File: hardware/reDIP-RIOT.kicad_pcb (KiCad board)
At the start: 4 copper layers, 17.8 x 50.8 mm, 45 parts, among them J1 Conn_01x20, J2 Conn_01x20, J3 Conn_02x05_Odd_Even, U1 NCP115AMX120TCG, U2 NCP115AMX330TCG, U3 SN74CBT16210CDGGR, U4 SN74CBT16210CDGGR, U5 74AHC1G14SE-7, U6 ICE5LP1K-SG48, U7 AT25EU0011A-SSHN-T

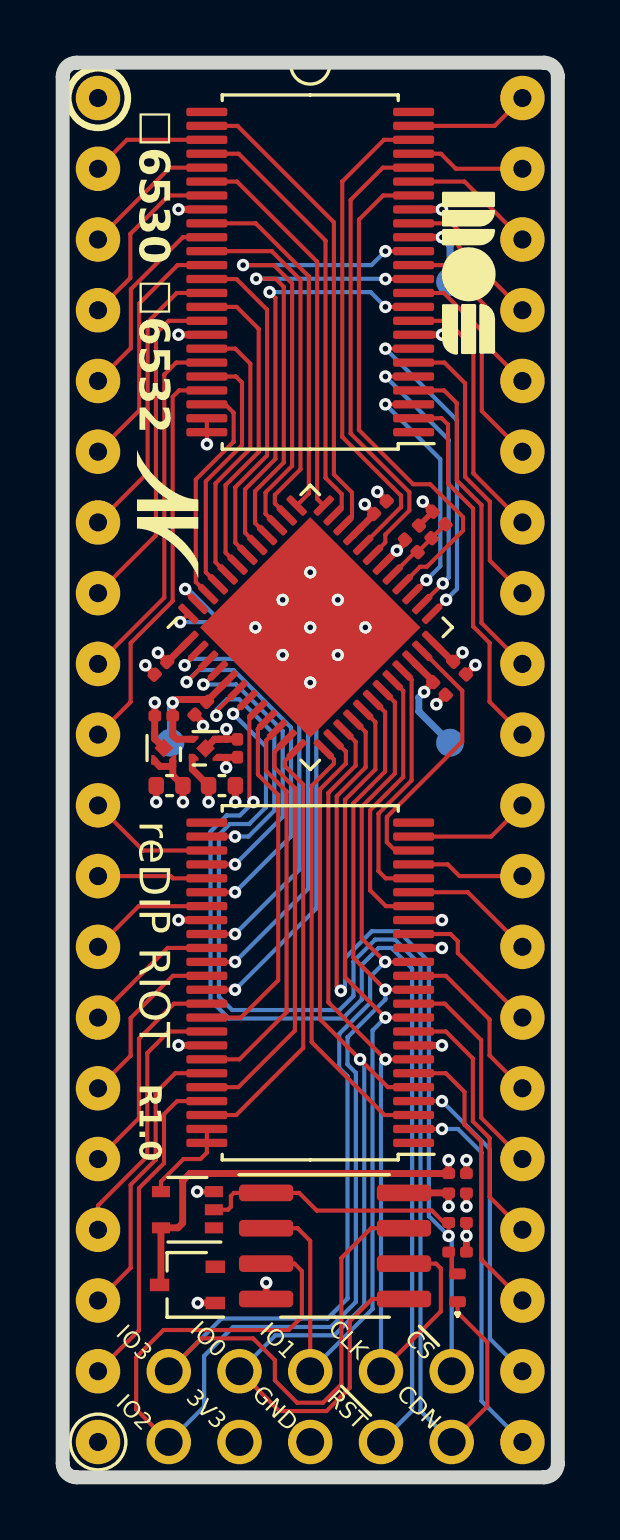
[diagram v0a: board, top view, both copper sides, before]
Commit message: Added CRESET pull-up, removed CDONE LED
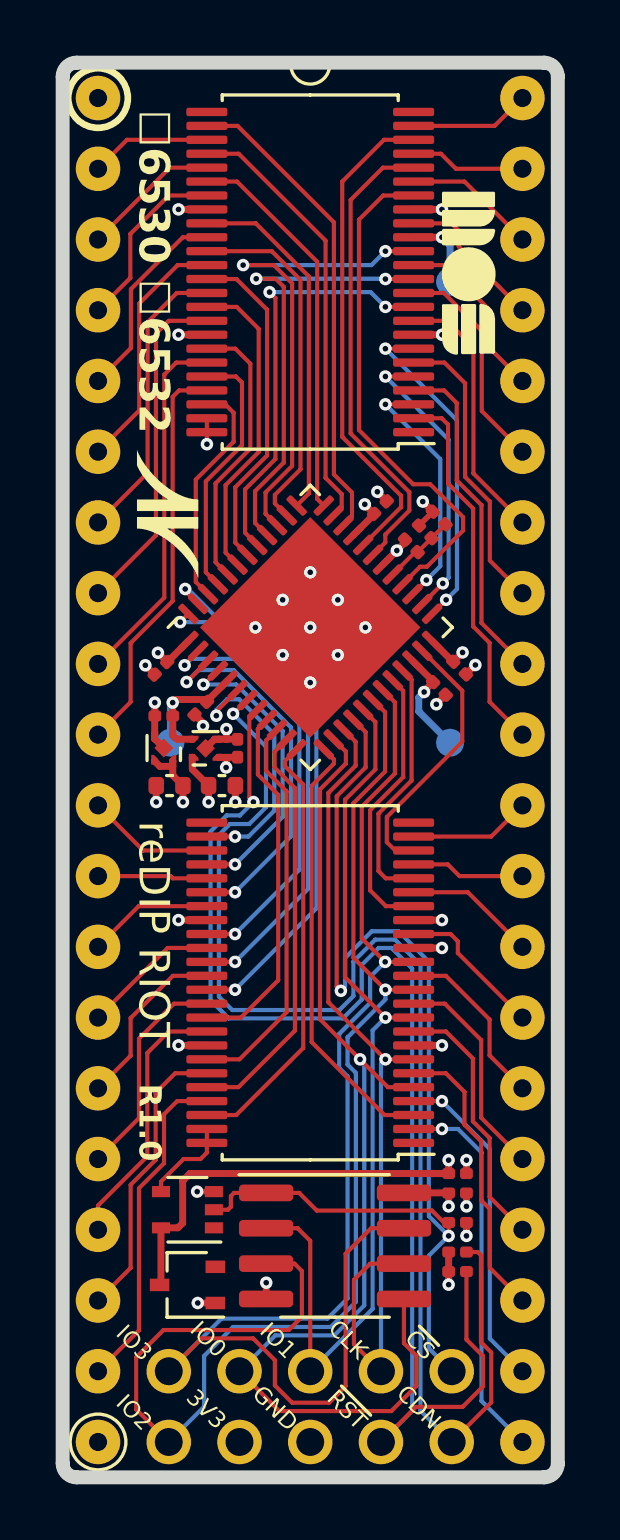
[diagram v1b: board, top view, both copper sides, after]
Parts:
- removed D2: IN-S42BT5B, Inolux:LED_0402_1005Metric
- removed the R3 at (112.9, 141.4)
- added R4: 10k, Resistor_SMD:R_0201_0603Metric, F.Cu at (112.9, 142.1)
- added R5: 2.87k, Resistor_SMD:R_0201_0603Metric, F.Cu at (112.9, 141.4)
- U5: value 74AHC1G14SE-7 -> 74AHC1G14
- renumbered R4 to R3
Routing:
- net /~{CRESET}: track 38.6 -> 47.4 mm
- net /CDONE: track 45.7 -> 47.7 mm
- net /SPI_SIO0: track 38.9 -> 40.0 mm
- net Net-(D2-A): track 0.96 -> 0.00 mm
- net /SPI_~{CS}: track 40.4 -> 41.0 mm
- net +3V3: track 12.8 -> 13.4 mm, vias 7 -> 8

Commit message: Cleanup
* Removed unused footprints
* Rounded rectangle pads for SOT footprints
* Increased drill to 0.8mm for header pins
* Corrected BOM text
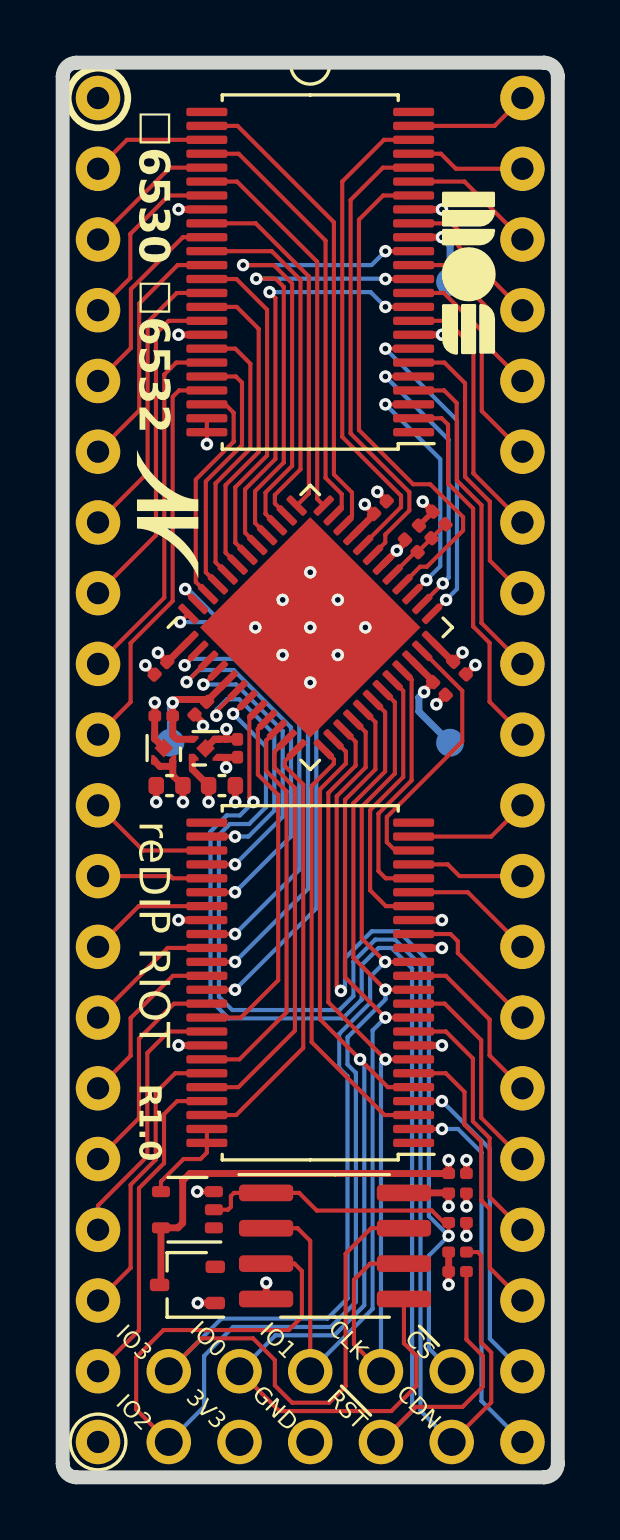
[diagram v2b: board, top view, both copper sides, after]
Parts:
- D1: footprint Package_TO_SOT_SMD:SOT-323_SC-70 -> reDIP:SOT-323_SC-70
- REF**: renamed from svg2mod; value G*** -> Nimrod N
- REF** (x2): renamed from MOS logo; value G*** -> MOS logo
- REF**: renamed from OSHW logo; value G*** -> OSHW logo
- REF**: renamed from svg2mod; value G*** -> Nimrod logo
- U5: footprint Package_TO_SOT_SMD:SOT-353_SC-70-5 -> reDIP:SOT-353_SC-70-5
- U7: value AT25EU0011A-SSHN-T -> AT25EU0011A-SSHN

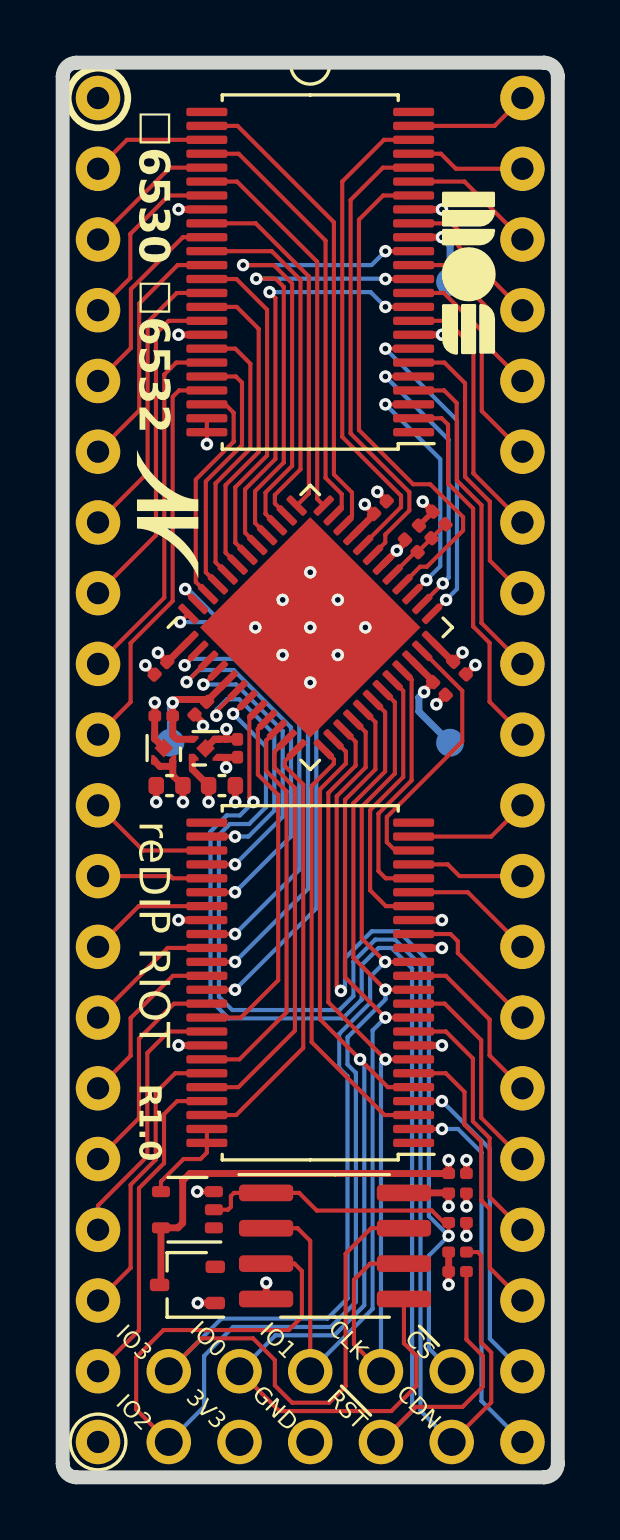
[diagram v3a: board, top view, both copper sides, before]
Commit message: LDO ground planes, via teardrops
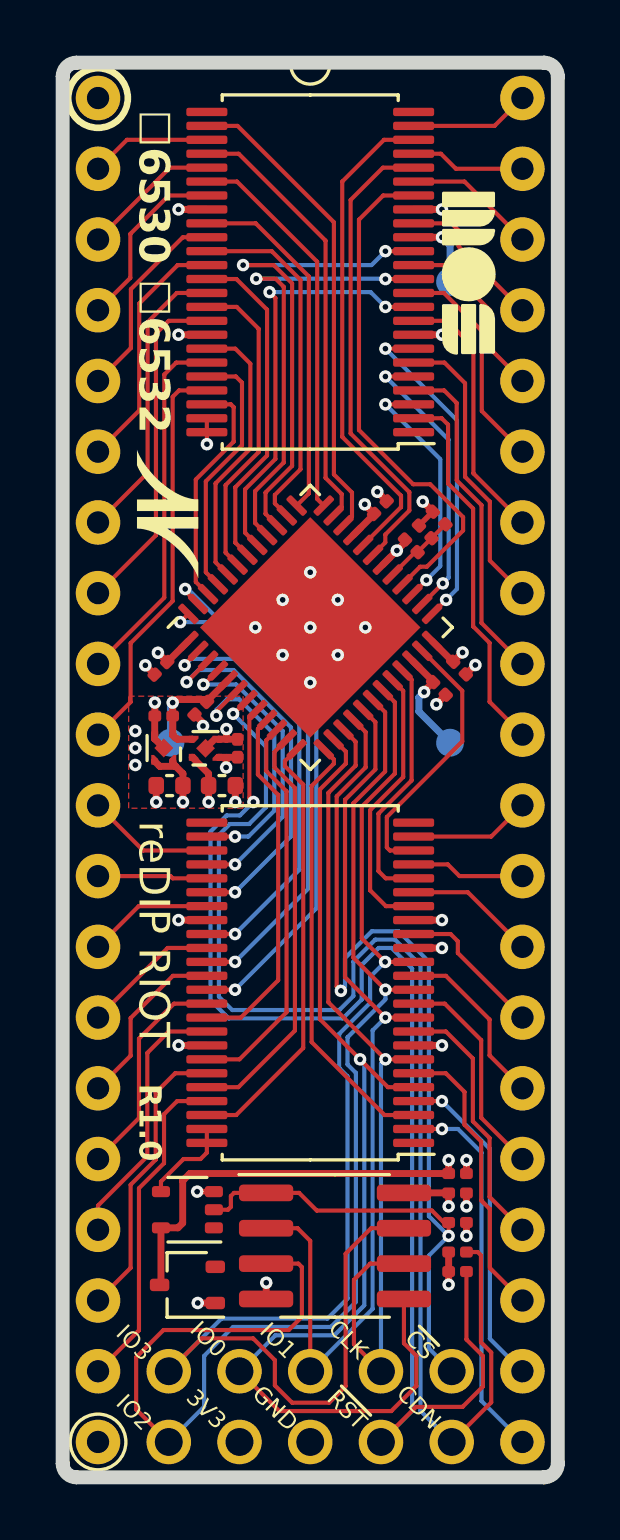
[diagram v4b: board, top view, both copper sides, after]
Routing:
- net GND: track 19.5 -> 19.4 mm, vias 32 -> 35
- added copper zone on F.Cu, net GND

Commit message: Use 74AHCT1G14 for better signal level margins
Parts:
- U5: value 74AHC1G14 -> 74AHCT1G14
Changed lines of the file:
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@@
     (property "Description" "IC SCHMITT-TRIGGER INVERTER")
     (property "Mfg" "Diodes")
-    (property "Notes" "Replacement parts: 74AHC1G14 SOT-353/SC-70-5")
-    (property "PN" "74AHC1G14SE-7")
+    (property "Notes" "Replacement parts: 74AHCT1G14 SOT-353/SC-70-5")
+    (property "PN" "74AHCT1G14SE-7")
     (property "Sheetfile" "reDIP-RIOT.kicad_sch")
     (property "Sheetname" "")
@@
         (effects (font (size 1 1) (thickness 0.15)))
     )
-    (fp_text value "74AHC1G14" (at 0 2) (layer "F.Fab") hide
+    (fp_text value "74AHCT1G14" (at 0 2) (layer "F.Fab") hide
         (effects (font (size 1 1) (thickness 0.15)))
     )

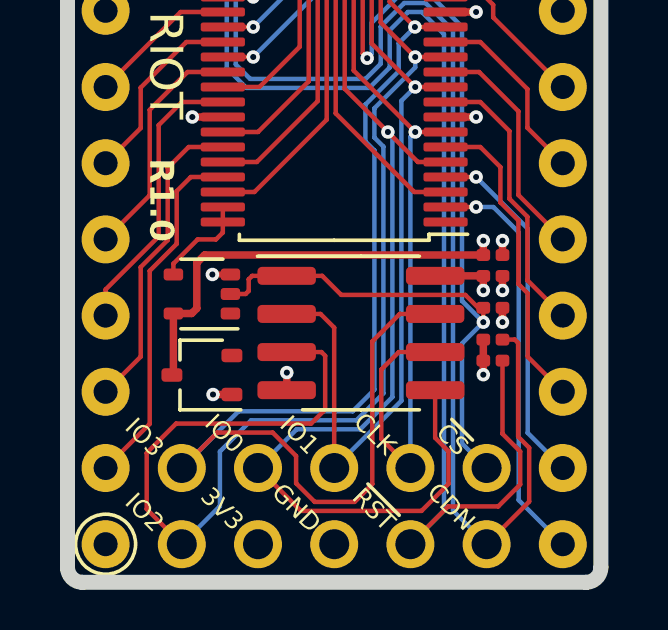
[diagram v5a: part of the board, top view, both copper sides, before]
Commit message: Power supply for 74AHCT1G14 within range
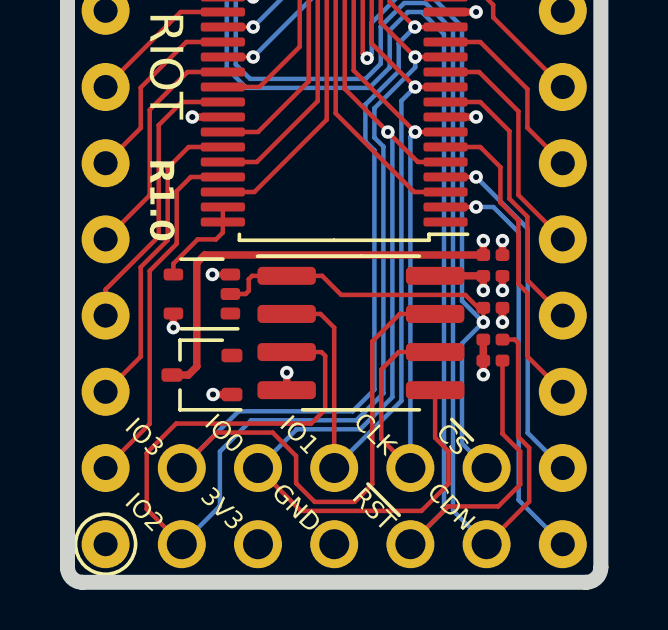
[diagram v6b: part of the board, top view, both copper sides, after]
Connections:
- U5 pad 5: VCBT -> VCC
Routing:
- net VCC: track 32.0 -> 32.3 mm, vias 3 -> 4

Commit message: Replaced iCE5LP1K with iCE40UP5K
The MOS 6530 and MOS 6532 have on-chip data port pull-up resistors
in the range of 5k.

While the iCE40UP5K features configurable 3.3k/6.8k/10k/100k pull-up
resistors, the iCE5LP1K only features 100k pull-up resistors.

We make the simple fix of using the more capable (and somewhat more
expensive) pin compatible iCE40UP5K, instead of adding physical
pull-up resistors to separate boards for the MOS 6530 and MOS 6532.
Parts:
- U6: value ICE5LP1K-SG48 -> ICE40UP5K-SG48
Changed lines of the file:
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@@
     (property "Description" "IC FPGA QFN-48")
     (property "Mfg" "Lattice")
-    (property "PN" "ICE5LP1K-SG48ITR")
+    (property "PN" "ICE40UP5K-SG48I")
     (property "Sheetfile" "reDIP-RIOT.kicad_sch")
     (property "Sheetname" "")
-    (property "ki_description" "iCE40 Ultra FPGA, 1100 LUTs, 1.2V, 48-pin QFN")
+    (property "ki_description" "iCE40 UltraPlus FPGA, 5280 LUTs, 1.2V, 48-pin QFN")
     (property "ki_keywords" "FPGA programmable logic")
     (attr smd)
@@
         (effects (font (size 1 1) (thickness 0.15)))
     )
-    (fp_text value "ICE5LP1K-SG48" (at 0 4.82 45) (layer "F.Fab") hide
+    (fp_text value "ICE40UP5K-SG48" (at 0 4.82 45) (layer "F.Fab") hide
         (effects (font (size 1 1) (thickness 0.15)))
     )
@@
     (pad "" smd roundrect (at 0 0 225) (size 0.38 0.38) (layers "F.Paste") (roundrect_rratio 0.2))
     (pad "1" smd custom (at -0.475 -0.325 90) (size 0.25 0.25) (layers "F.Cu" "F.Paste" "F.Mask")
-      (net 2 "+3V3") (pinfunction "OUT") (pintype "power_out") (zone_connect 2) (thermal_bridge_angle 45)
+      (net 2 "+3V3") (pinfunction "OUT") (pintype "power_out") (zone_connect 2)
       (options (clearance outline) (anchor circle))
       (primitives
@@
       ))
     (pad "2" smd custom (at -0.475 0.325 270) (size 0.25 0.25) (layers "F.Cu" "F.Paste" "F.Mask")
-      (net 1 "GND") (pinfunction "GND") (pintype "power_in") (zone_connect 2) (thermal_bridge_angle 45)
+      (net 1 "GND") (pinfunction "GND") (pintype "power_in") (zone_connect 2)
       (options (clearance outline) (anchor circle))
       (primitives
@@
       (net 1 "GND") (pinfunction "GND") (pintype "power_in"))
     (pad "3" smd custom (at 0.475 0.325 270) (size 0.25 0.25) (layers "F.Cu" "F.Paste" "F.Mask")
-      (net 3 "+1V2") (pinfunction "EN") (pintype "input") (zone_connect 2) (thermal_bridge_angle 45)
+      (net 3 "+1V2") (pinfunction "EN") (pintype "input") (zone_connect 2)
       (options (clearance outline) (anchor circle))
       (primitives
@@
       ))
     (pad "4" smd custom (at 0.475 -0.325 90) (size 0.25 0.25) (layers "F.Cu" "F.Paste" "F.Mask")
-      (net 17 "VCC") (pinfunction "IN") (pintype "power_in") (zone_connect 2) (thermal_bridge_angle 45)
+      (net 17 "VCC") (pinfunction "IN") (pintype "power_in") (zone_connect 2)
       (options (clearance outline) (anchor circle))
       (primitives
@@
     (pad "" smd roundrect (at 0 0 315) (size 0.38 0.38) (layers "F.Paste") (roundrect_rratio 0.2))
     (pad "1" smd custom (at -0.475 -0.325 180) (size 0.25 0.25) (layers "F.Cu" "F.Paste" "F.Mask")
-      (net 3 "+1V2") (pinfunction "OUT") (pintype "power_out") (zone_connect 2) (thermal_bridge_angle 45)
+      (net 3 "+1V2") (pinfunction "OUT") (pintype "power_out") (zone_connect 2)
       (options (clearance outline) (anchor circle))
       (primitives
@@
       ))
     (pad "2" smd custom (at -0.475 0.325) (size 0.25 0.25) (layers "F.Cu" "F.Paste" "F.Mask")
-      (net 1 "GND") (pinfunction "GND") (pintype "power_in") (zone_connect 2) (thermal_bridge_angle 45)
+      (net 1 "GND") (pinfunction "GND") (pintype "power_in") (zone_connect 2)
       (options (clearance outline) (anchor circle))
       (primitives
@@
       (net 1 "GND") (pinfunction "GND") (pintype "power_in"))
     (pad "3" smd custom (at 0.475 0.325) (size 0.25 0.25) (layers "F.Cu" "F.Paste" "F.Mask")
-      (net 17 "VCC") (pinfunction "EN") (pintype "input") (zone_connect 2) (thermal_bridge_angle 45)
+      (net 17 "VCC") (pinfunction "EN") (pintype "input") (zone_connect 2)
       (options (clearance outline) (anchor circle))
       (primitives
@@
       ))
     (pad "4" smd custom (at 0.475 -0.325 180) (size 0.25 0.25) (layers "F.Cu" "F.Paste" "F.Mask")
-      (net 17 "VCC") (pinfunction "IN") (pintype "power_in") (zone_connect 2) (thermal_bridge_angle 45)
+      (net 17 "VCC") (pinfunction "IN") (pintype "power_in") (zone_connect 2)
       (options (clearance outline) (anchor circle))
       (primitives
@@
   (via (at 103.97 125.28) (size 0.45) (drill 0.2) (layers "F.Cu" "B.Cu") (free) (net 17))
   (via (at 103.58 143.27) (size 0.45) (drill 0.2) (layers "F.Cu" "B.Cu") (net 17))
-  (segment (start 102.26 142.98) (end 102.55 143.27) (width 0.45) (layer "In2.Cu") (net 17))
-  (segment (start 102.26 141.04) (end 102.26 142.98) (width 0.45) (layer "In2.Cu") (net 17))
+  (segment (start 102.26 141.04) (end 102.26 143.27) (width 0.45) (layer "In2.Cu") (net 17))
+  (segment (start 102.26 143.27) (end 101.27 144.26) (width 0.45) (layer "In2.Cu") (net 17))
   (segment (start 103.05 125.28) (end 103.51 125.28) (width 0.45) (layer "In2.Cu") (net 17))
   (segment (start 103.51 125.28) (end 103.97 125.28) (width 0.45) (layer "In2.Cu") (net 17))
@@
   (segment (start 102.26 141.04) (end 102.26 127.41) (width 0.45) (layer "In2.Cu") (net 17))
   (segment (start 102.26 127.41) (end 103.51 126.16) (width 0.45) (layer "In2.Cu") (net 17))
+  (segment (start 101.27 144.26) (end 101.27 146.99) (width 0.45) (layer "In2.Cu") (net 17))
   (segment (start 103.51 125.28) (end 103.51 126.16) (width 0.45) (layer "In2.Cu") (net 17))
-  (segment (start 101.27 143.97) (end 101.27 146.99) (width 0.45) (layer "In2.Cu") (net 17))
-  (segment (start 101.27 143.97) (end 102.26 142.98) (width 0.45) (layer "In2.Cu") (net 17))
-  (segment (start 102.55 143.27) (end 103.58 143.27) (width 0.45) (layer "In2.Cu") (net 17))
+  (segment (start 102.26 143.27) (end 103.58 143.27) (width 0.45) (layer "In2.Cu") (net 17))
   (segment (start 113.48 108.95) (end 113.48 113.48) (width 0.15) (layer "F.Cu") (net 18))
   (segment (start 113.48 113.48) (end 115.24 115.24) (width 0.15) (layer "F.Cu") (net 18))
@@
         (xy 98.73 149.53)
         (xy 98.73 125.05)
-        (xy 104.2 125.05)
-        (xy 104.21 149.53)
+        (xy 103.76 125.05)
+        (xy 103.73 149.53)
       )
     )
